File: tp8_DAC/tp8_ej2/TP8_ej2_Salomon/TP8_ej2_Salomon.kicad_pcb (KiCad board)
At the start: 2 copper layers, 21 parts, among them J1 alimentacion, J2 input, J3 output, Q1 BC548, Q2 BC547, Q3 BC548

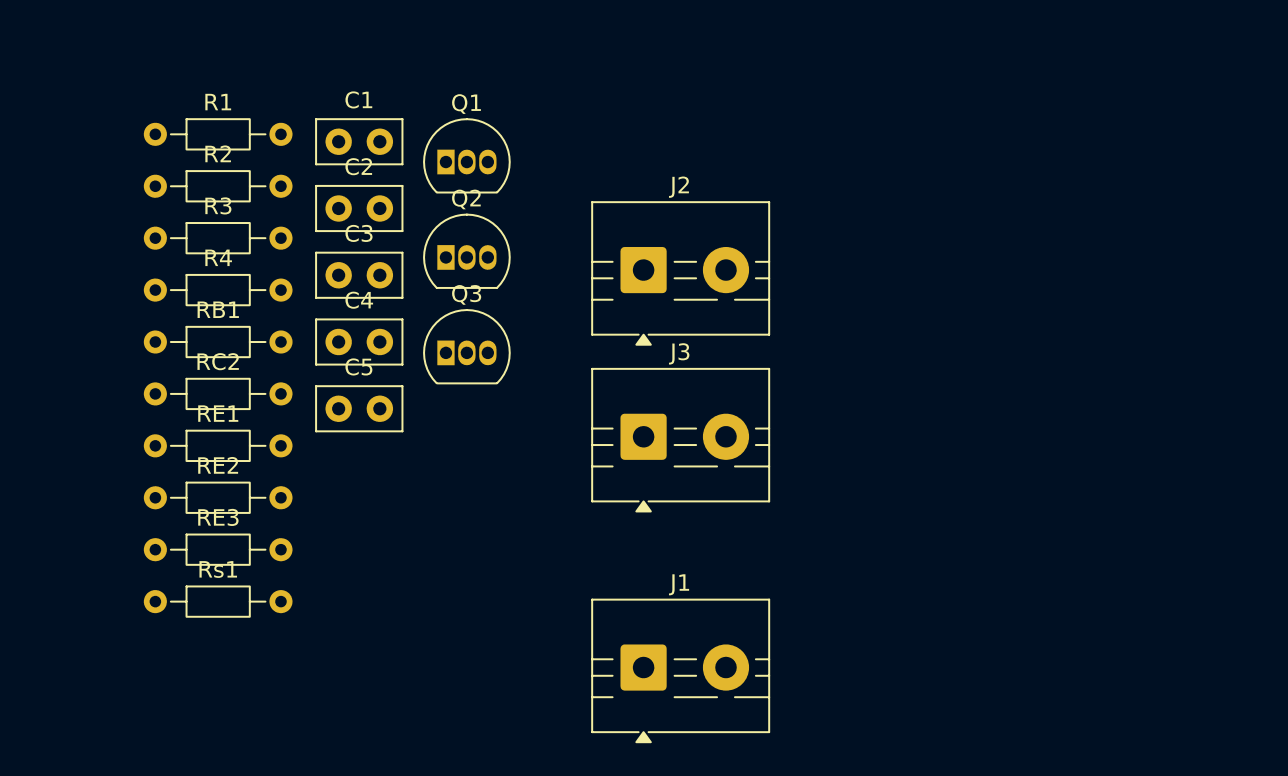
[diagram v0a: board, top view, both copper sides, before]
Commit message: update_schematics_ej2
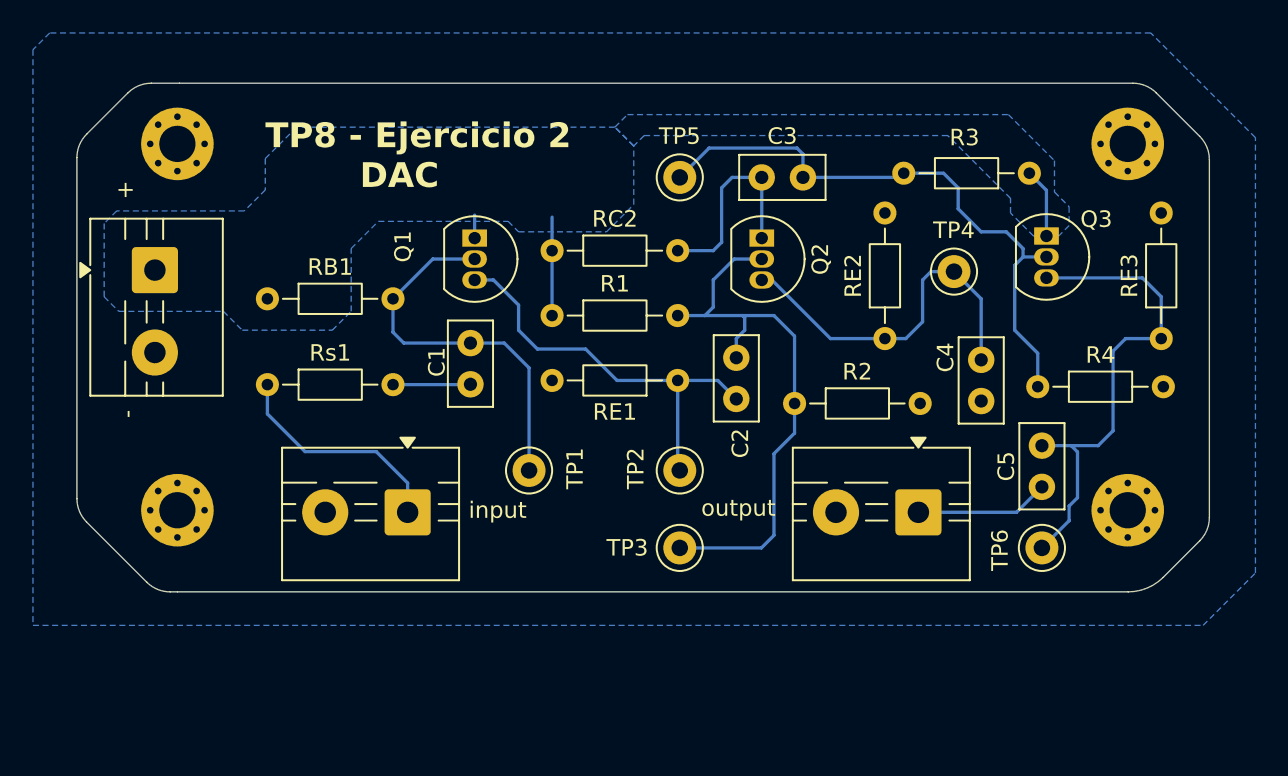
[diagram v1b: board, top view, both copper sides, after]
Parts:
- added H1: MountingHole_Pad, MountingHole:MountingHole_2.2mm_M2_Pad_Via, F.Cu at (198.4, 70.2)
- added H2: MountingHole_Pad, MountingHole:MountingHole_2.2mm_M2_Pad_Via, F.Cu at (198.4, 92.5)
- added H3: MountingHole_Pad, MountingHole:MountingHole_2.2mm_M2_Pad_Via, B.Cu at (140.7, 70.2)
- added H4: MountingHole_Pad, MountingHole:MountingHole_2.2mm_M2_Pad_Via, F.Cu at (140.7, 92.5)
- added TP1: TestPoint_Alt, TestPoint:TestPoint_Keystone_5000-5004_Miniature, F.Cu at (162.1, 90.0)
- added TP2: TestPoint_Alt, TestPoint:TestPoint_Keystone_5000-5004_Miniature, F.Cu at (171.2, 90.0)
- added TP3: TestPoint_Alt, TestPoint:TestPoint_Keystone_5000-5004_Miniature, F.Cu at (171.2, 94.7)
- added TP4: TestPoint_Alt, TestPoint:TestPoint_Keystone_5000-5004_Miniature, F.Cu at (187.8, 78.0)
- added TP5: TestPoint_Alt, TestPoint:TestPoint_Keystone_5000-5004_Miniature, F.Cu at (171.2, 72.3)
- added TP6: TestPoint_Alt, TestPoint:TestPoint_Keystone_5000-5004_Miniature, F.Cu at (193.2, 94.7)
- moved RE3 62.4 mm to (200.4, 82.0), turned to 90 degrees
- moved R4 53.9 mm to (192.9, 85.0)
- moved R3 53.2 mm to (192.4, 72.0), turned to 180 degrees
- moved RE2 45.3 mm to (183.6, 82.0), turned to 90 degrees
- moved C5 42.7 mm to (193.2, 88.5), turned to -90 degrees
- moved R2 41.0 mm to (178.2, 86.0)
- moved C4 39.0 mm to (189.5, 83.3), turned to -90 degrees
- moved + 38.2 mm to (139.4, 77.9), turned to -90 degrees
- moved Q3 37.1 mm to (193.4, 75.8), turned to -90 degrees
- moved RE1 31.9 mm to (171.1, 84.6), turned to 180 degrees
- moved C2 26.7 mm to (174.6, 85.7), turned to 90 degrees
- moved R1 26.5 mm to (163.4, 80.6)
- moved C3 26.3 mm to (176.2, 72.3)
- moved RC2 25.6 mm to (163.4, 76.7)
- moved input 20.5 mm to (154.7, 92.6), turned to 180 degrees
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- renumbered J1 to +, J2 to input, J3 to output
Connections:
- + pad 1: Net-(J1-Pin_1) -> +9V
- Q1 pad 1: Net-(Q1-C) -> +9V
- Q3 pad 1: Net-(Q1-C) -> +9V
- R1 pad 1: Net-(Q1-C) -> +9V
- R3 pad 1: Net-(Q1-C) -> +9V
- RB1 pad 1: Net-(Q1-C) -> +9V
- RC2 pad 1: Net-(Q1-C) -> +9V
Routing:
- net Net-(Q3-B): track 0.00 -> 36.5 mm
- net Net-(Q2-B): track 0.00 -> 34.9 mm
- net Net-(Q3-E): track 0.00 -> 30.0 mm
- net Net-(Q1-E): track 0.00 -> 25.3 mm
- net Net-(Q1-B): track 0.00 -> 23.4 mm
- net Net-(Q2-E): track 0.00 -> 22.3 mm
- net Net-(J2-Pin_1): track 0.00 -> 13.8 mm
- net Net-(Q2-C): track 0.00 -> 12.6 mm
- net +9V: track 0.00 -> 11.6 mm
- net Net-(J3-Pin_1): track 0.00 -> 8.13 mm
- net Net-(C1-Pad1): track 0.00 -> 4.71 mm
- added copper zone on B.Cu, net +9V
- added copper zone on B.Cu, net GND
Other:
- board outline added: 68.7 x 30.9 mm
- board text added: "-"
- board text added: "TP8 - Ejercicio 2 DAC"

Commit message: update_final
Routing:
- net Net-(Q2-C): track 12.6 -> 9.10 mm
- net Net-(Q1-B): track 23.4 -> 24.2 mm
